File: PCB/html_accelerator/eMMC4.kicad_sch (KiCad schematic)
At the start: 14 parts, among them U10 AU6438BS, U11 EMMC_4G, Y5 12MHz

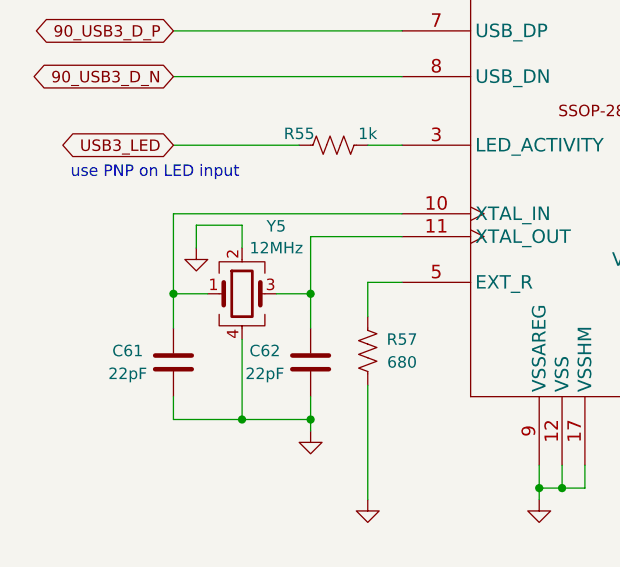
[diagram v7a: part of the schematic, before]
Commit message: Additional routing greebles, cleanup and gerber export with BOM
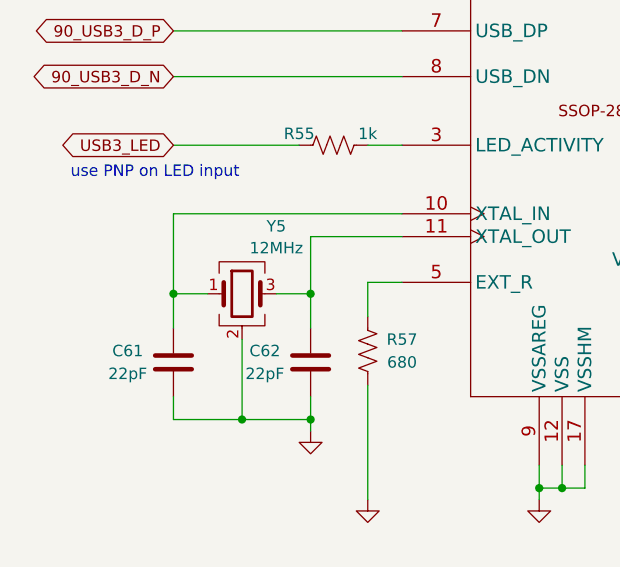
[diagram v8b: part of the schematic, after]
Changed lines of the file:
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@@
-	(wire
-		(pts
-			(xy 36.83 87.63) (xy 36.83 90.17)
-		)
-		(stroke
-			(width 0)
-			(type default)
-		)
-	)
 	(wire
 		(pts
@@
 	(wire
 		(pts
-			(xy 41.91 90.17) (xy 41.91 87.63)
-		)
-		(stroke
-			(width 0)
-			(type default)
-		)
-	)
-	(wire
-		(pts
 			(xy 113.03 88.9) (xy 114.3 88.9)
 		)
@@
 		(pts
 			(xy 59.69 66.04) (xy 34.29 66.04)
-		)
-		(stroke
-			(width 0)
-			(type default)
-		)
-	)
-	(wire
-		(pts
-			(xy 41.91 87.63) (xy 36.83 87.63)
 		)
 		(stroke
@@
 	)
 	(symbol
-		(lib_id "power:GND")
-		(at 36.83 90.17 0)
-		(unit 1)
-		(body_style 1)
-		(exclude_from_sim no)
-		(in_bom yes)
-		(on_board yes)
-		(in_pos_files yes)
-		(dnp no)
-		(fields_autoplaced yes)
-		(property "Reference" "#PWR059"
-			(at 36.83 96.52 0)
-			(hide yes)
-			(show_name no)
-			(do_not_autoplace no)
-			(effects
-				(font
-					(size 1.27 1.27)
-				)
-			)
-		)
-		(property "Value" "GND"
-			(at 36.83 94.3055 0)
-			(hide yes)
-			(show_name no)
-			(do_not_autoplace no)
-			(effects
-				(font
-					(size 1.27 1.27)
-				)
-			)
-		)
-		(property "Footprint" ""
-			(at 36.83 90.17 0)
-			(hide yes)
-			(show_name no)
-			(do_not_autoplace no)
-			(effects
-				(font
-					(size 1.27 1.27)
-				)
-			)
-		)
-		(property "Datasheet" ""
-			(at 36.83 90.17 0)
-			(hide yes)
-			(show_name no)
-			(do_not_autoplace no)
-			(effects
-				(font
-					(size 1.27 1.27)
-				)
-			)
-		)
-		(property "Description" ""
-			(at 36.83 90.17 0)
-			(show_name no)
-			(do_not_autoplace no)
-			(effects
-				(font
-					(size 1.27 1.27)
-				)
-			)
-		)
-		(pin "1"
-		)
-		(instances
-			(project "html_accelerator"
-				(path "/12b3a7c9-141f-40ba-9ebb-094b58bfa6c7/e85df621-c9d6-4c41-83df-274e70c69afa"
-					(reference "#PWR059")
-					(unit 1)
-				)
-			)
-		)
-	)
-	(symbol
 		(lib_id "Device:C")
 		(at 49.53 102.87 0)
@@
 			)
 		)
-		(property "Description" ""
+		(property "Description" "Four pin crystal, GND on pins 2 and 4"
 			(at 41.91 95.25 0)
-			(show_name no)
-			(do_not_autoplace no)
+			(hide yes)
+			(show_name no)
+			(do_not_autoplace no)
